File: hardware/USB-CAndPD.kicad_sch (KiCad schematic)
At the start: 31 parts, among them J201 USB_C_Receptacle_USB2.0_16P, J202 USB_C_Receptacle_USB2.0_16P, U201 TPS25730D, U202 TPD2E2U06DCK

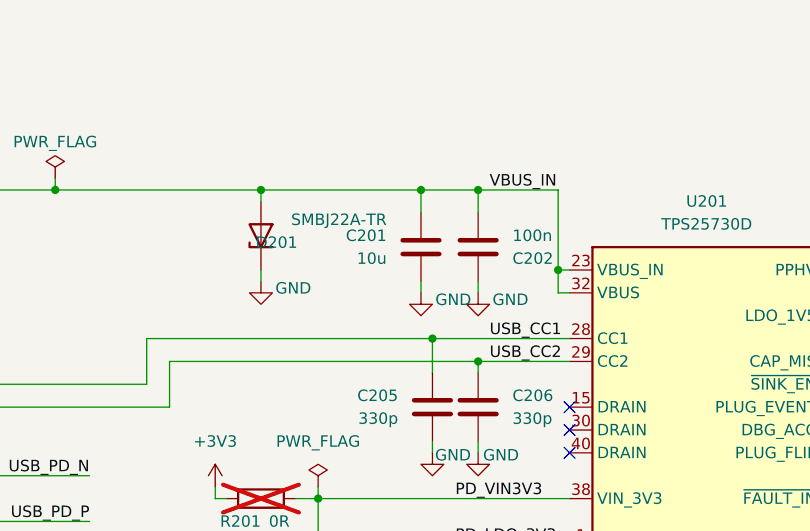
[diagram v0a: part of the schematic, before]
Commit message: Thermal reliefes
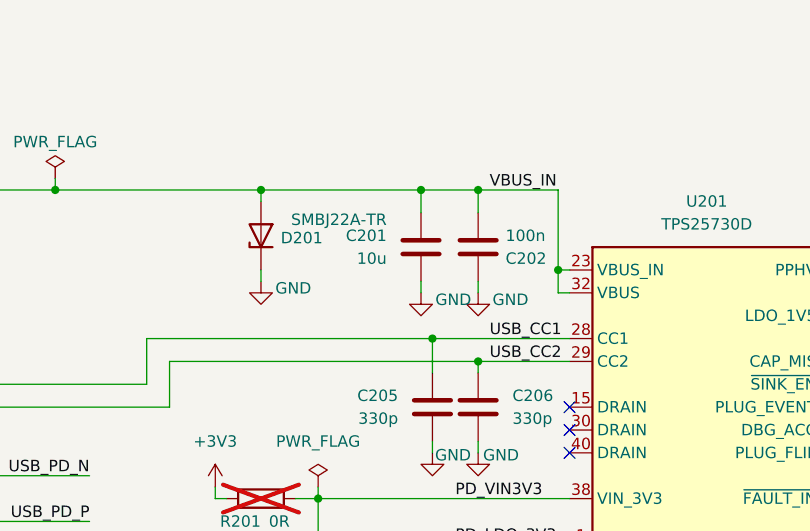
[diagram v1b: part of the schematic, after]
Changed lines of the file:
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@@
 		(dnp no)
 		(property "Reference" "C202"
-			(at 130.81 40.6401 0)
+			(at 130.048 40.64 0)
 			(effects
 				(font
@@
 		)
 		(property "Value" "100n"
-			(at 130.81 38.1001 0)
+			(at 130.048 38.1 0)
 			(effects
 				(font
@@
 		(dnp no)
 		(property "Reference" "D201"
-			(at 106.934 38.862 90)
+			(at 109.728 38.354 90)
 			(effects
 				(font

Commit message: Exchanged 5k11 with 5k1 part number
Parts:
- R206, R212, R213, R214: ManufacturerNumber RT0603DRE075K11L -> RC0603FR-105K1L; MouserNumber 603-RT0603DRE075K11L -> 603-RC0603FR-105K1L
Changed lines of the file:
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@@
 			)
 		)
-		(property "MouserNumber" "603-RT0603DRE075K11L"
+		(property "MouserNumber" "603-RC0603FR-105K1L"
 			(at 214.63 119.38 0)
 			(effects
@@
 			)
 		)
-		(property "ManufacturerNumber" "RT0603DRE075K11L"
+		(property "ManufacturerNumber" "RC0603FR-105K1L"
 			(at 214.63 119.38 0)
 			(effects
@@
 			)
 		)
-		(property "MouserNumber" "603-RT0603DRE075K11L"
+		(property "MouserNumber" "603-RC0603FR-105K1L"
 			(at 214.63 86.36 0)
 			(effects
@@
 			)
 		)
-		(property "ManufacturerNumber" "RT0603DRE075K11L"
+		(property "ManufacturerNumber" "RC0603FR-105K1L"
 			(at 214.63 86.36 0)
 			(effects
@@
 			)
 		)
-		(property "MouserNumber" "603-RT0603DRE075K11L"
+		(property "MouserNumber" "603-RC0603FR-105K1L"
 			(at 97.79 119.38 0)
 			(effects
@@
 			)
 		)
-		(property "ManufacturerNumber" "RT0603DRE075K11L"
+		(property "ManufacturerNumber" "RC0603FR-105K1L"
 			(at 97.79 119.38 90)
 			(effects
@@
 			)
 		)
-		(property "MouserNumber" "603-RT0603DRE075K11L"
+		(property "MouserNumber" "603-RC0603FR-105K1L"
 			(at 90.17 119.38 0)
 			(effects
@@
 			)
 		)
-		(property "ManufacturerNumber" "RT0603DRE075K11L"
+		(property "ManufacturerNumber" "RC0603FR-105K1L"
 			(at 90.17 119.38 90)
 			(effects
